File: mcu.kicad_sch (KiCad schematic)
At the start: 19 parts, among them J2 Conn_01x06, J3 Conn_01x02, U1 TPS73233DBVR, U3 STM32G070xB

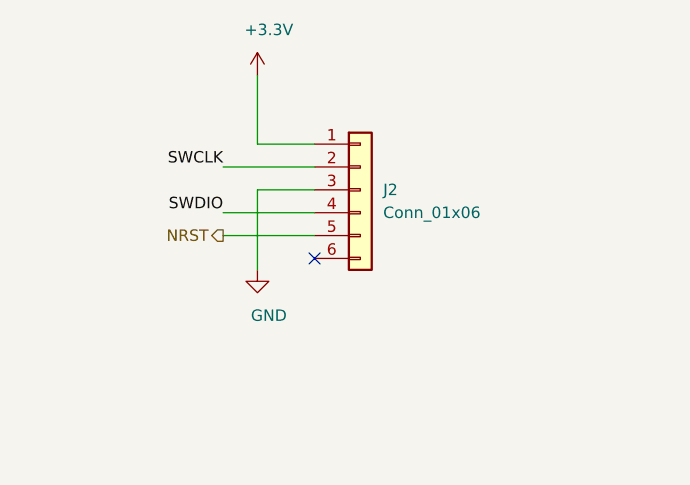
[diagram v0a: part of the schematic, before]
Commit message: Replaced Picoblade connector with standard pin header Updated libraries to KiCAD 6 format
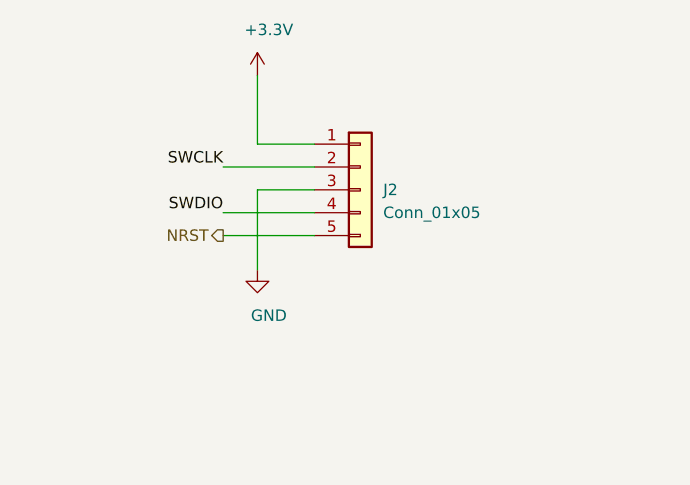
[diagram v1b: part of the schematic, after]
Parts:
- J2: value Conn_01x06 -> Conn_01x05; footprint Connector_Molex:Molex_PicoBlade_53047-0610_1x06_P1.25mm_Vertical -> Connector_PinHeader_2.54mm:PinHeader_1x05_P2.54mm_Vertical; symbol Connector_Generic:Conn_01x06 -> Connector_Generic:Conn_01x05; MFN Molex -> Amphenol FCI; PN 53047-0610 -> 10129380-905001BLF
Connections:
- no-connect marks 1 -> 0
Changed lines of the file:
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@@
   (junction (at 85.09 33.02) (diameter 0) (color 0 0 0 0)
   )
-  (no_connect (at 234.95 48.26))
   (wire (pts (xy 194.31 140.97) (xy 194.31 139.7))
     (stroke (width 0) (type default) (color 0 0 0 0))
@@
     (pin "9")
   )
-  (symbol (lib_id "Connector_Generic:Conn_01x06") (at 240.03 40.64 0) (unit 1)
+  (symbol (lib_id "Connector_Generic:Conn_01x05") (at 240.03 40.64 0) (unit 1)
     (in_bom yes) (on_board yes)
     (property "Reference" "J2" (id 0) (at 242.57 40.64 0)
       (effects (font (size 1.27 1.27)) (justify left))
     )
-    (property "Value" "Conn_01x06" (id 1) (at 242.57 43.18 0)
+    (property "Value" "Conn_01x05" (id 1) (at 242.57 43.18 0)
       (effects (font (size 1.27 1.27)) (justify left))
     )
-    (property "Footprint" "Connector_Molex:Molex_PicoBlade_53047-0610_1x06_P1.25mm_Vertical" (id 2) (at 240.03 40.64 0)
+    (property "Footprint" "Connector_PinHeader_2.54mm:PinHeader_1x05_P2.54mm_Vertical" (id 2) (at 240.03 40.64 0)
       (effects (font (size 1.27 1.27)) hide)
     )
@@
       (effects (font (size 1.27 1.27)) hide)
     )
-    (property "MFN" "Molex" (id 4) (at 240.03 40.64 0)
-      (effects (font (size 1.27 1.27)) hide)
-    )
-    (property "PN" "53047-0610" (id 5) (at 240.03 40.64 0)
+    (property "MFN" "Amphenol FCI" (id 4) (at 240.03 40.64 0)
+      (effects (font (size 1.27 1.27)) hide)
+    )
+    (property "PN" "10129380-905001BLF" (id 5) (at 240.03 40.64 0)
       (effects (font (size 1.27 1.27)) hide)
     )
@@
     (pin "4")
     (pin "5")
-    (pin "6")
   )
   (symbol (lib_id "power:+3.3V") (at 228.6 27.94 0) (unit 1)

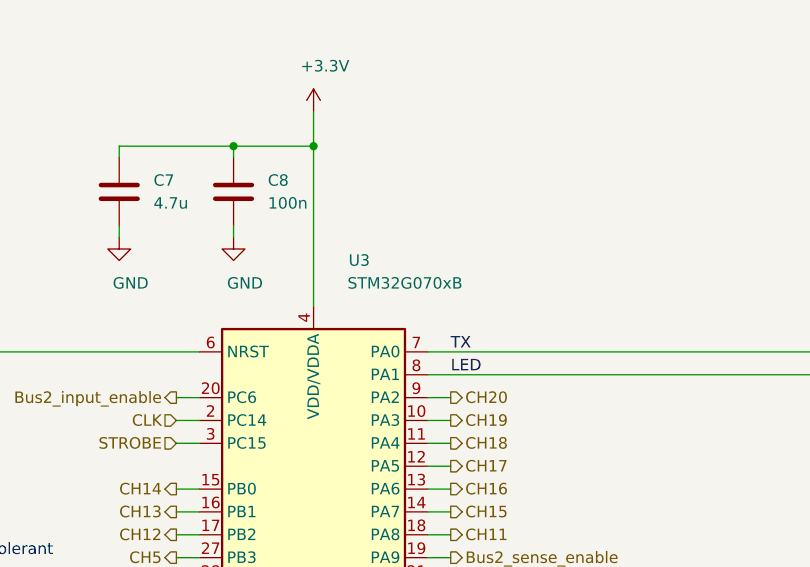
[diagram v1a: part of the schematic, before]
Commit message: Updated silkscreen
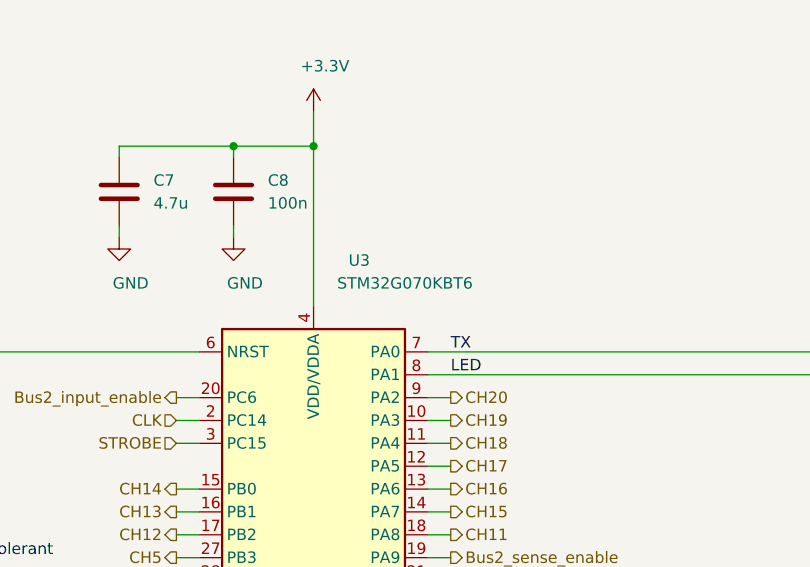
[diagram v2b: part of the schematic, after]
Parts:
- U3: value STM32G070xB -> STM32G070KBT6
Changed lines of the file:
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@@
     (in_bom yes) (on_board yes)
     (property "Reference" "U3" (id 0) (at 170.18 83.82 0))
-    (property "Value" "STM32G070xB" (id 1) (at 175.26 86.36 0))
+    (property "Value" "STM32G070KBT6" (id 1) (at 175.26 86.36 0))
     (property "Footprint" "Package_QFP:LQFP-32_7x7mm_P0.8mm" (id 2) (at 154.94 134.62 0)
       (effects (font (size 1.27 1.27)) (justify right) hide)
